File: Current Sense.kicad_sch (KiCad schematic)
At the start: 3 parts, among them U2 ACS711xLCTR-12AB

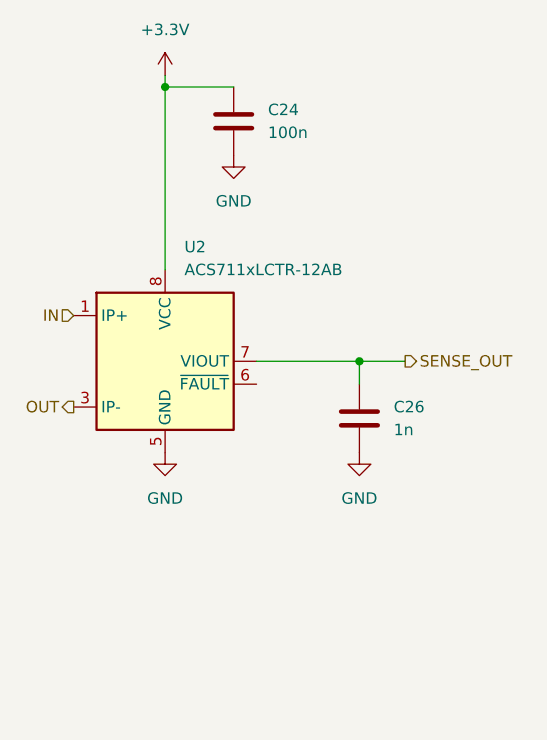
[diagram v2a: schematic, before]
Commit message: schematic changes and initial routing
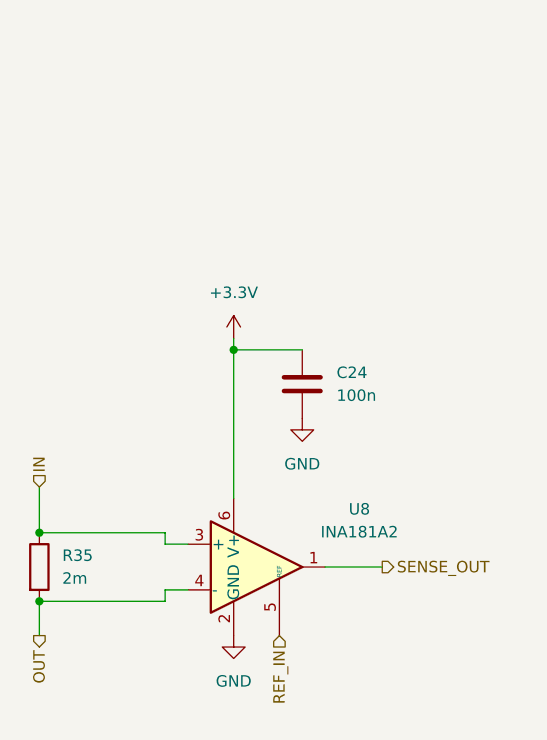
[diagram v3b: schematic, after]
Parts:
- removed C26: 1n, Capacitor_SMD:C_0603_1608Metric_Pad1.08x0.95mm_HandSolder, symbol Device:C
- removed U2: ACS711xLCTR-12AB, Package_SO:SOIC-8_3.9x4.9mm_P1.27mm, symbol Sensor_Current:ACS711xLCTR-12AB
- added R35: 2m, Resistor_SMD:R_1206_3216Metric_Pad1.30x1.75mm_HandSolder, symbol Device:R
- added U8: INA181A2, Package_TO_SOT_SMD:SOT-23-6_Handsoldering, symbol Amplifier_Current:INA181
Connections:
- net +3.3V: now also U8.6 (V+)
- net GND: now also U8.2 (GND)
- net IN: now also R35.1, U8.3 (+)
- net OUT: now also R35.2, U8.4 (-)
- net SENSE_OUT: now also U8.1
- new net REF_IN: U8.5 (REF)

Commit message: finished layout, routing, and silkscreen
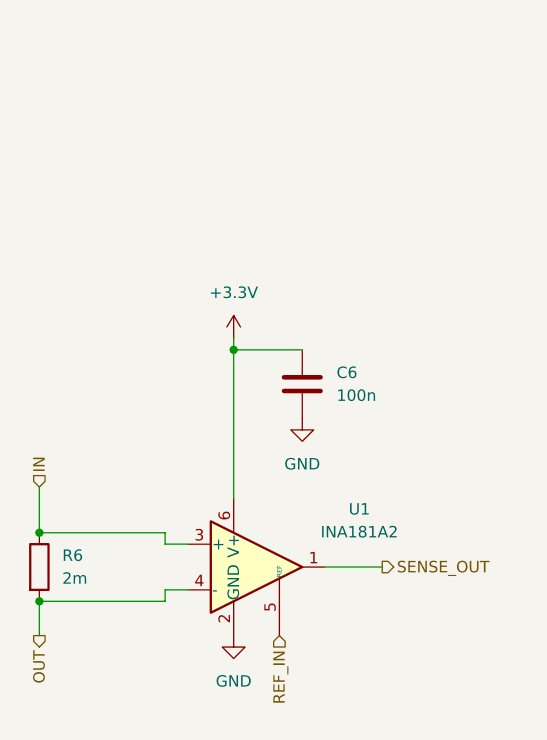
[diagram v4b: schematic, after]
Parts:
- renumbered C24 to C6, R35 to R6, U8 to U1
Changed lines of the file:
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@@
 		(dnp no)
 		(fields_autoplaced yes)
-		(property "Reference" "#PWR059"
+		(property "Reference" "#PWR014"
 			(at 144.78 118.11 0)
 			(hide yes)
@@
 			(project "RSC-LV3-LVBPS"
 				(path "/4bbf2fff-9f66-421d-84bf-68d1dcd1e11d/c1fc57fb-2a25-4f9b-b603-c1810d2158c8"
-					(reference "#PWR060")
-					(unit 1)
-				)
-				(path "/4bbf2fff-9f66-421d-84bf-68d1dcd1e11d/db786f64-50ae-4c36-99a3-24972523a002"
-					(reference "#PWR059")
+					(reference "#PWR017")
+					(unit 1)
+				)
+				(path "/4bbf2fff-9f66-421d-84bf-68d1dcd1e11d/db786f64-50ae-4c36-99a3-24972523a002"
+					(reference "#PWR014")
 					(unit 1)
 				)
@@
 		(dnp no)
 		(fields_autoplaced yes)
-		(property "Reference" "U8"
+		(property "Reference" "U1"
 			(at 158.75 97.7198 0)
 			(show_name no)
@@
 			(project "RSC-LV3-LVBPS"
 				(path "/4bbf2fff-9f66-421d-84bf-68d1dcd1e11d/c1fc57fb-2a25-4f9b-b603-c1810d2158c8"
-					(reference "U9")
-					(unit 1)
-				)
-				(path "/4bbf2fff-9f66-421d-84bf-68d1dcd1e11d/db786f64-50ae-4c36-99a3-24972523a002"
-					(reference "U8")
+					(reference "U2")
+					(unit 1)
+				)
+				(path "/4bbf2fff-9f66-421d-84bf-68d1dcd1e11d/db786f64-50ae-4c36-99a3-24972523a002"
+					(reference "U1")
 					(unit 1)
 				)
@@
 		(dnp no)
 		(fields_autoplaced yes)
-		(property "Reference" "C24"
+		(property "Reference" "C6"
 			(at 156.21 82.5499 0)
 			(show_name no)
@@
 			(project "RSC-LV3-LVBPS"
 				(path "/4bbf2fff-9f66-421d-84bf-68d1dcd1e11d/c1fc57fb-2a25-4f9b-b603-c1810d2158c8"
-					(reference "C25")
-					(unit 1)
-				)
-				(path "/4bbf2fff-9f66-421d-84bf-68d1dcd1e11d/db786f64-50ae-4c36-99a3-24972523a002"
-					(reference "C24")
+					(reference "C7")
+					(unit 1)
+				)
+				(path "/4bbf2fff-9f66-421d-84bf-68d1dcd1e11d/db786f64-50ae-4c36-99a3-24972523a002"
+					(reference "C6")
 					(unit 1)
 				)
@@
 		(dnp no)
 		(fields_autoplaced yes)
-		(property "Reference" "#PWR055"
+		(property "Reference" "#PWR013"
 			(at 144.78 82.55 0)
 			(hide yes)
@@
 			(project "RSC-LV3-LVBPS"
 				(path "/4bbf2fff-9f66-421d-84bf-68d1dcd1e11d/c1fc57fb-2a25-4f9b-b603-c1810d2158c8"
-					(reference "#PWR056")
-					(unit 1)
-				)
-				(path "/4bbf2fff-9f66-421d-84bf-68d1dcd1e11d/db786f64-50ae-4c36-99a3-24972523a002"
-					(reference "#PWR055")
+					(reference "#PWR016")
+					(unit 1)
+				)
+				(path "/4bbf2fff-9f66-421d-84bf-68d1dcd1e11d/db786f64-50ae-4c36-99a3-24972523a002"
+					(reference "#PWR013")
 					(unit 1)
 				)
@@
 		(dnp no)
 		(fields_autoplaced yes)
-		(property "Reference" "R35"
+		(property "Reference" "R6"
 			(at 125.73 102.8699 0)
 			(show_name no)
@@
 			(project "RSC-LV3-LVBPS"
 				(path "/4bbf2fff-9f66-421d-84bf-68d1dcd1e11d/c1fc57fb-2a25-4f9b-b603-c1810d2158c8"
-					(reference "R36")
-					(unit 1)
-				)
-				(path "/4bbf2fff-9f66-421d-84bf-68d1dcd1e11d/db786f64-50ae-4c36-99a3-24972523a002"
-					(reference "R35")
+					(reference "R7")
+					(unit 1)
+				)
+				(path "/4bbf2fff-9f66-421d-84bf-68d1dcd1e11d/db786f64-50ae-4c36-99a3-24972523a002"
+					(reference "R6")
 					(unit 1)
 				)
@@
 		(dnp no)
 		(fields_autoplaced yes)
-		(property "Reference" "#PWR057"
+		(property "Reference" "#PWR015"
 			(at 152.4 93.98 0)
 			(hide yes)
@@
 			(project "RSC-LV3-LVBPS"
 				(path "/4bbf2fff-9f66-421d-84bf-68d1dcd1e11d/c1fc57fb-2a25-4f9b-b603-c1810d2158c8"
-					(reference "#PWR058")
-					(unit 1)
-				)
-				(path "/4bbf2fff-9f66-421d-84bf-68d1dcd1e11d/db786f64-50ae-4c36-99a3-24972523a002"
-					(reference "#PWR057")
-					(unit 1)
-				)
+					(reference "#PWR018")
+					(unit 1)
+				)
+				(path "/4bbf2fff-9f66-421d-84bf-68d1dcd1e11d/db786f64-50ae-4c36-99a3-24972523a002"
+					(reference "#PWR015")
+					(unit 1)
+				)
